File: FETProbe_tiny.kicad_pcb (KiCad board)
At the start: 2 copper layers, 23 x 15 mm, 17 parts, among them J1 u.Fl, J5 u.Fl, Q1 BF998

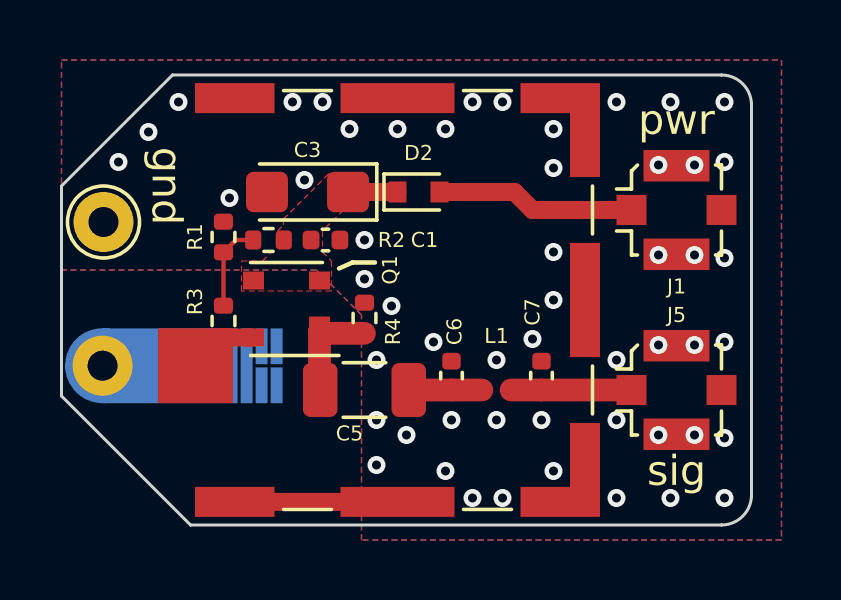
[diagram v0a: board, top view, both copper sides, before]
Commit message: feat: Added bottom silkscreen with project info.
Also rotated designators on top silkscreen to all face the same way,
and added @mpb27 to remind me of the fork.
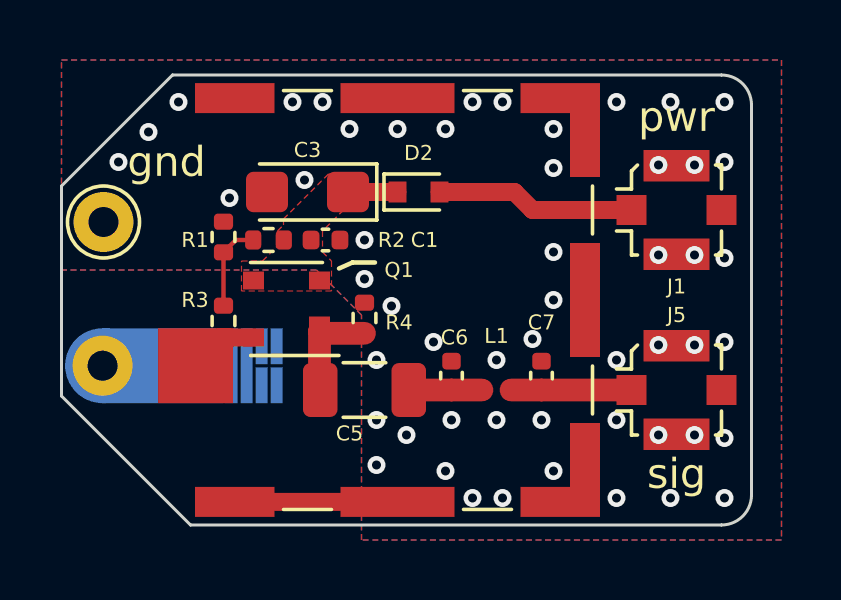
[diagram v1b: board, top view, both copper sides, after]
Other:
- board text added: "1.3GHz"
- board text added: "FETProbe_tiny @crteensy"
- board text added: "rev. @mpb27"
